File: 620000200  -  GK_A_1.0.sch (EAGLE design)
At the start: 64 parts, among them IC1 PIC18F26K22, IC6 REG1117, Q1 16MHz, Q2 12MHz, T1 BCR505-W, T2 BCR505-W, U1 74AHC1G08DBV, U3 74AHC1G32DBV

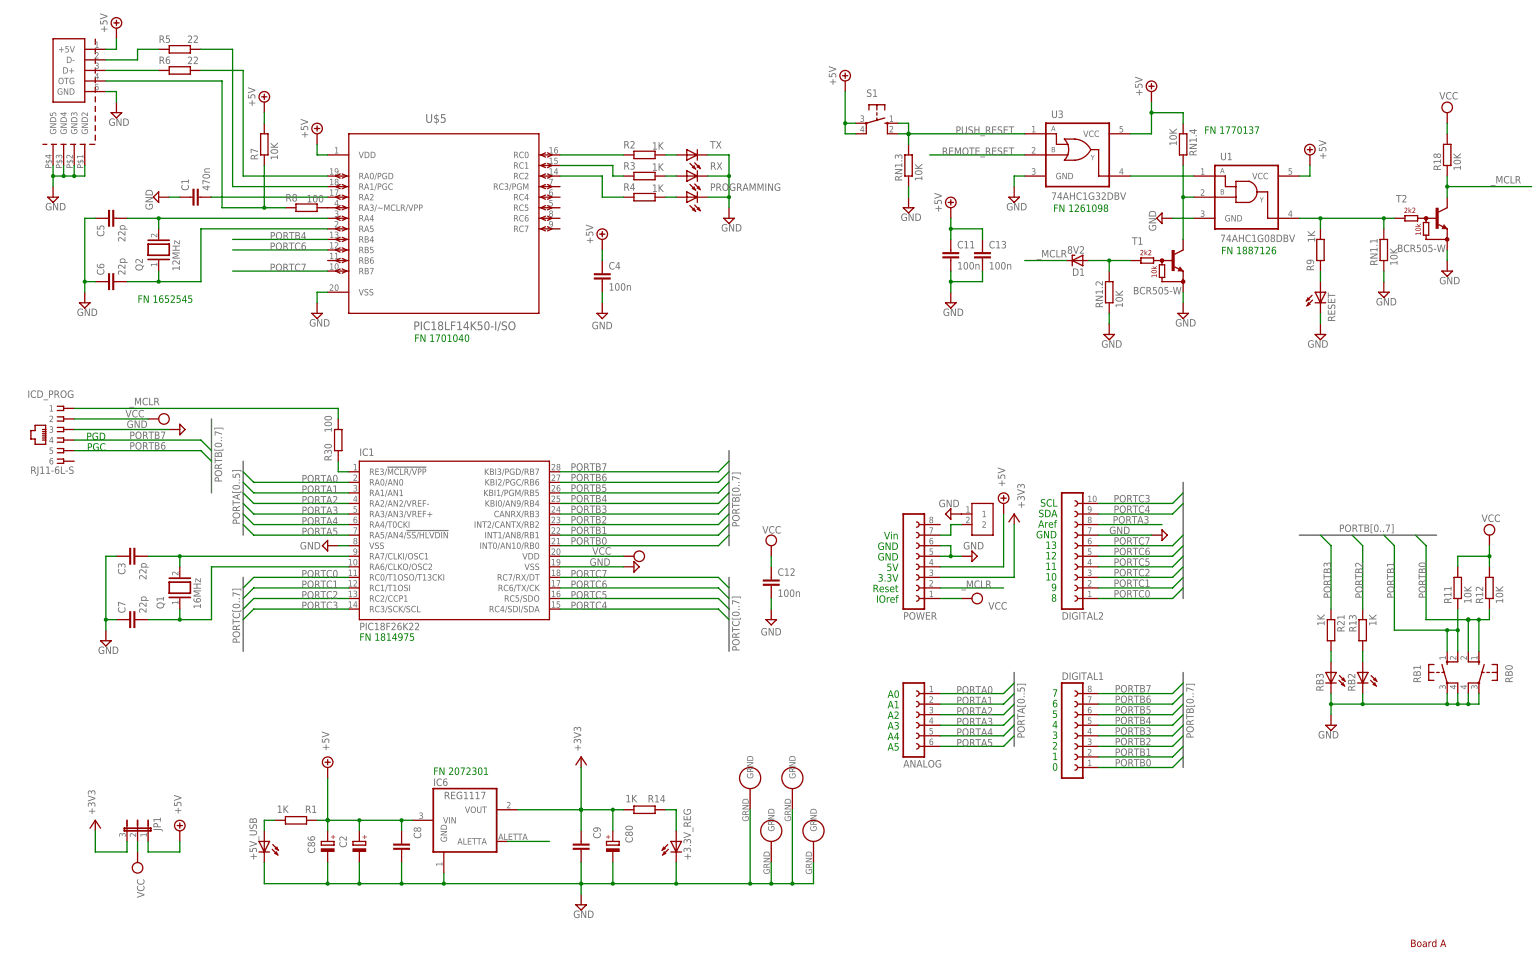
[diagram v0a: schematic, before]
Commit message: Progetto pronto per rifare con le nuove MCU. Mantenuto : Alimentazione Reset Struttura arduino compatibile
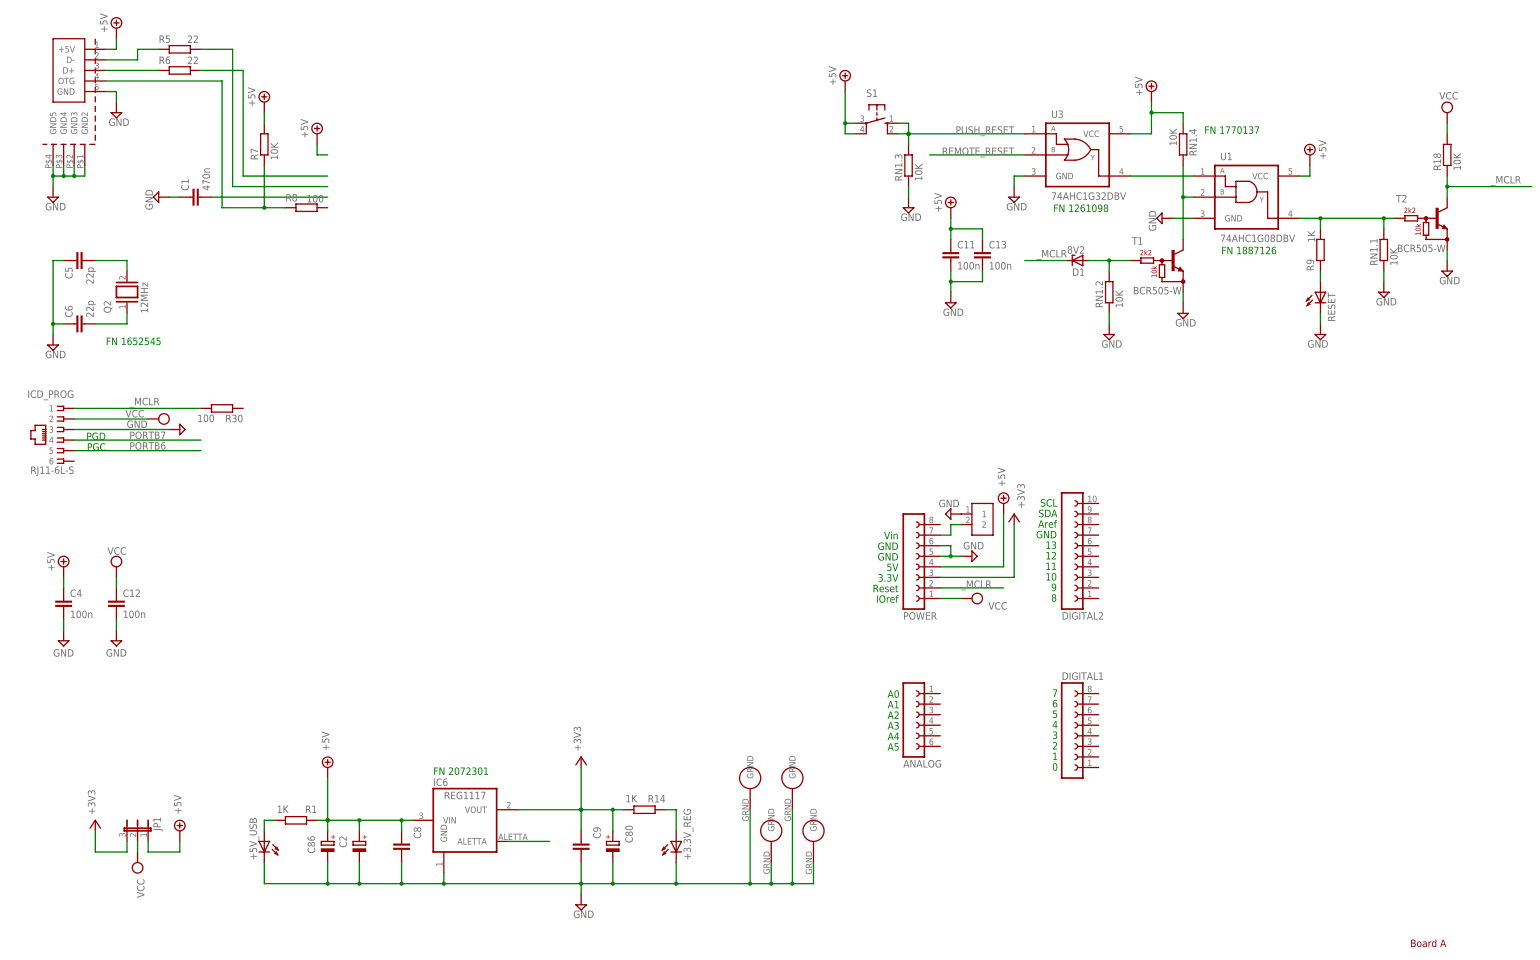
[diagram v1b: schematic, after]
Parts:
- removed C3, C7: 22p, rcl:C-EUC0805
- removed IC1: PIC18F26K22, microchip:PIC18F2480-I/SP
- removed PROGRAMMING, RB2, RB3, RX, TX: (no value), led:LEDCHIPLED_0805
- removed Q1: 16MHz, special:XTAL/S
- removed R11, R12: 10K, rcl:R-EU_R0805
- removed R13, R2, R21, R3, R4: 1K, rcl:R-EU_R0805
- removed RB0, RB1: (no value), switch-omron:10-XX
- removed U$5: PIC18LF14K50-I/SO, gkripthw:PIC18LF14K50-I/SO
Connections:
- removed net N$1: IC1.RE3/!MCLR/VPP, R30.2
- removed net N$15: R2.2, U$5.RC0
- removed net N$16: R3.2, U$5.RC1
- removed net N$17: R2.1, TX.A
- removed net N$18: R3.1, RX.A
- removed net N$21: C3.2, IC1.RA7/CLKI/OSC1, Q1.2
- removed net N$22: C7.2, IC1.RA6/CLKO/OSC2, Q1.1
- removed net N$24: PROGRAMMING.A, R4.1
- removed net N$25: R4.2, U$5.RC2
- removed net N$28: R8.2, U$5.RA3/~MCLR/VPP
- removed net N$3: R21.2, RB3.A
- removed net N$5: R13.2, RB2.A
- removed net PORTA0: ANALOG.1, IC1.RA0/AN0
- removed net PORTA1: ANALOG.2, IC1.RA1/AN1
- removed net PORTA2: ANALOG.3, IC1.RA2/AN2/VREF-
- removed net PORTA3: ANALOG.4, DIGITAL2.8, IC1.RA3/AN3/VREF+
- removed net PORTA4: ANALOG.5, IC1.RA4/T0CKI
- removed net PORTA5: ANALOG.6, IC1.RA5/AN4/!SS/HLVDIN
- removed net PORTB0: DIGITAL1.1, IC1.INT0/AN10/RB0, R12.1, RB0.S, RB0.S1
- removed net PORTB1: DIGITAL1.2, IC1.INT1/AN8/RB1, R11.1, RB1.S, RB1.S1
- removed net PORTB2: DIGITAL1.3, IC1.INT2/CANTX/RB2, R13.1
- removed net PORTB3: DIGITAL1.4, IC1.CANRX/RB3, R21.1
- removed net PORTB4: DIGITAL1.5, IC1.KBI0/AN9/RB4, U$5.RB4
- removed net PORTB5: DIGITAL1.6, IC1.KBI1/PGM/RB5
- removed net PORTC0: DIGITAL2.1, IC1.RC0/T1OSO/T13CKI
- removed net PORTC1: DIGITAL2.2, IC1.RC1/T1OSI
- removed net PORTC2: DIGITAL2.3, IC1.RC2/CCP1
- removed net PORTC3: DIGITAL2.10, IC1.RC3/SCK/SCL
- removed net PORTC4: DIGITAL2.9, IC1.RC4/SDI/SDA
- removed net PORTC5: DIGITAL2.4, IC1.RC5/SDO
- removed net PORTC6: DIGITAL2.5, IC1.RC6/TX/CK, U$5.RB5
- removed net PORTC7: DIGITAL2.6, IC1.RC7/RX/DT, U$5.RB7
- net +5V: no longer U$5.VDD
- net GND: no longer C3.1, C7.1, DIGITAL2.7, IC1.VSS, IC1.VSS@1, PROGRAMMING.C, RB0.P, RB0.P1, RB1.P, RB1.P1, RB2.C, RB3.C, RX.C, TX.C, U$5.VSS
- net N$10: no longer U$5.RA0/PGD
- net N$13: no longer U$5.RA5
- net N$26: no longer U$5.RA2
- net N$8: no longer U$5.RA4
- net N$9: no longer U$5.RA1/PGC
- net PORTB6: no longer DIGITAL1.7, IC1.KBI2/PGC/RB6
- net PORTB7: no longer DIGITAL1.8, IC1.KBI3/PGD/RB7
- net VCC: no longer IC1.VDD, R11.2, R12.2
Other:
- note removed: "FN 1701040"
- note removed: "FN 1814975"
- moved on the sheet: C12, C4, C5, C6, Q2, R30
